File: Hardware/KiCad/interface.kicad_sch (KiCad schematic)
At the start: 36 parts, among them J2 STLink, J6 UART, J7 OLED, SW10 SW_Push_45deg, SW11 SW_Push_45deg, SW12 SW_Push_45deg, SW13 SW_Push_45deg, SW14 SW_Push_45deg, SW15 SW_Push_45deg, SW16 SW_Push_45deg, SW17 SW_Push_45deg, SW2 SW_Push_45deg, SW3 SW_Push_45deg, SW4 SW_Push_45deg, SW5 SW_Push_45deg, SW6 SW_Push_45deg, SW7 SW_Push_45deg, SW8 SW_Push_45deg, SW9 SW_Push_45deg

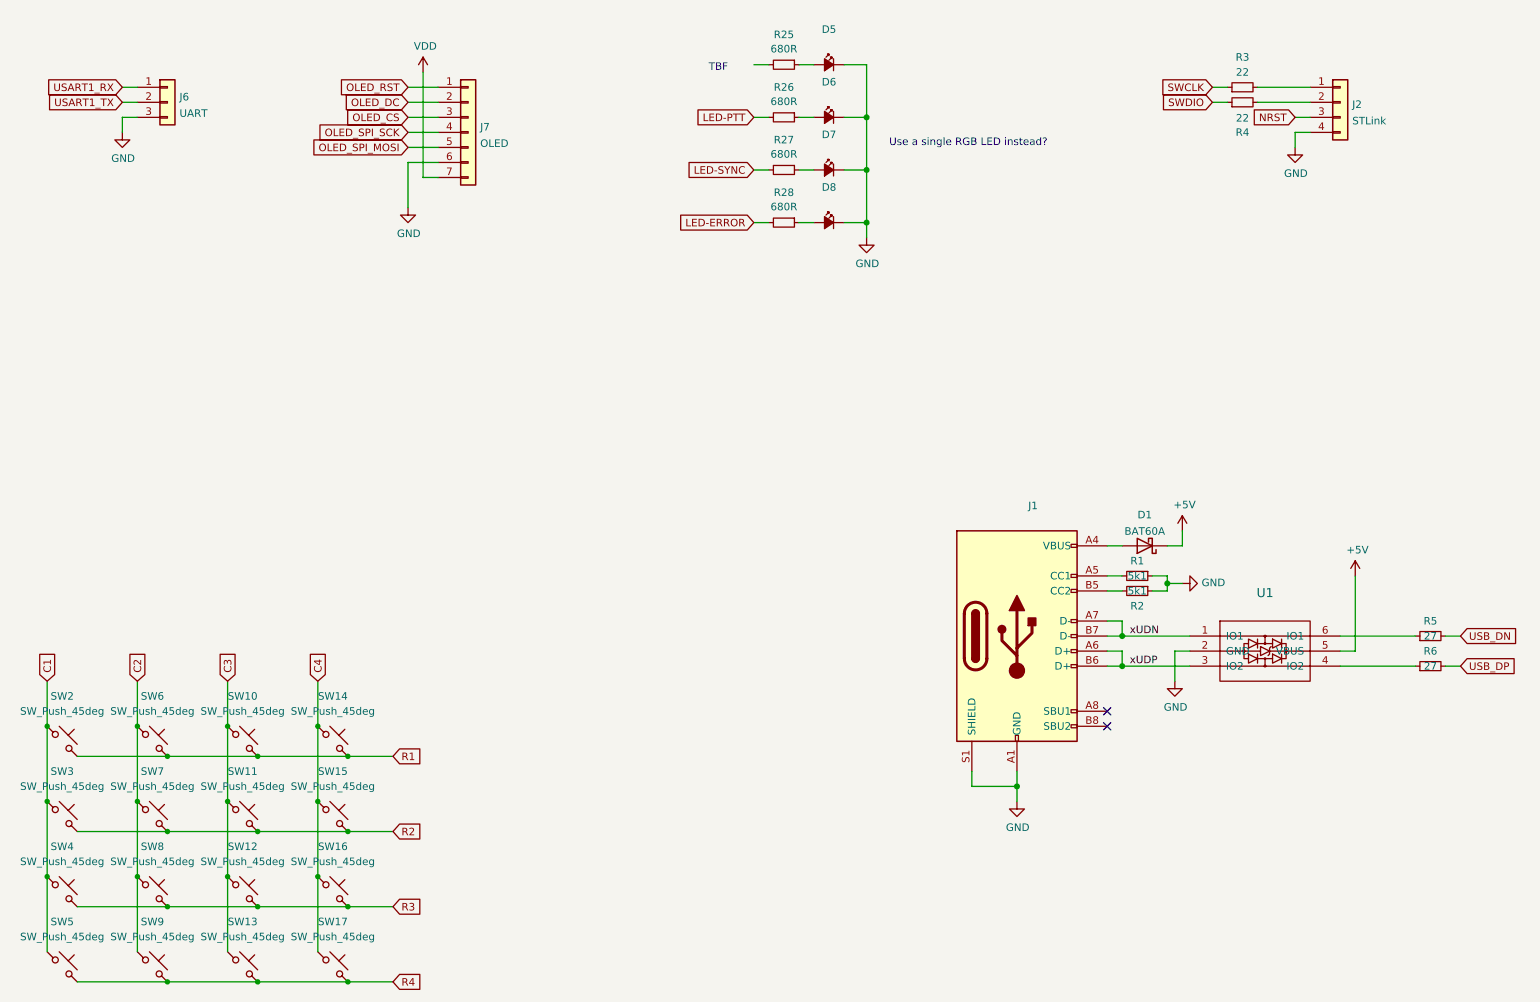
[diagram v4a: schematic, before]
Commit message: move cc1200 spi to spi-5 & update other labels throughout
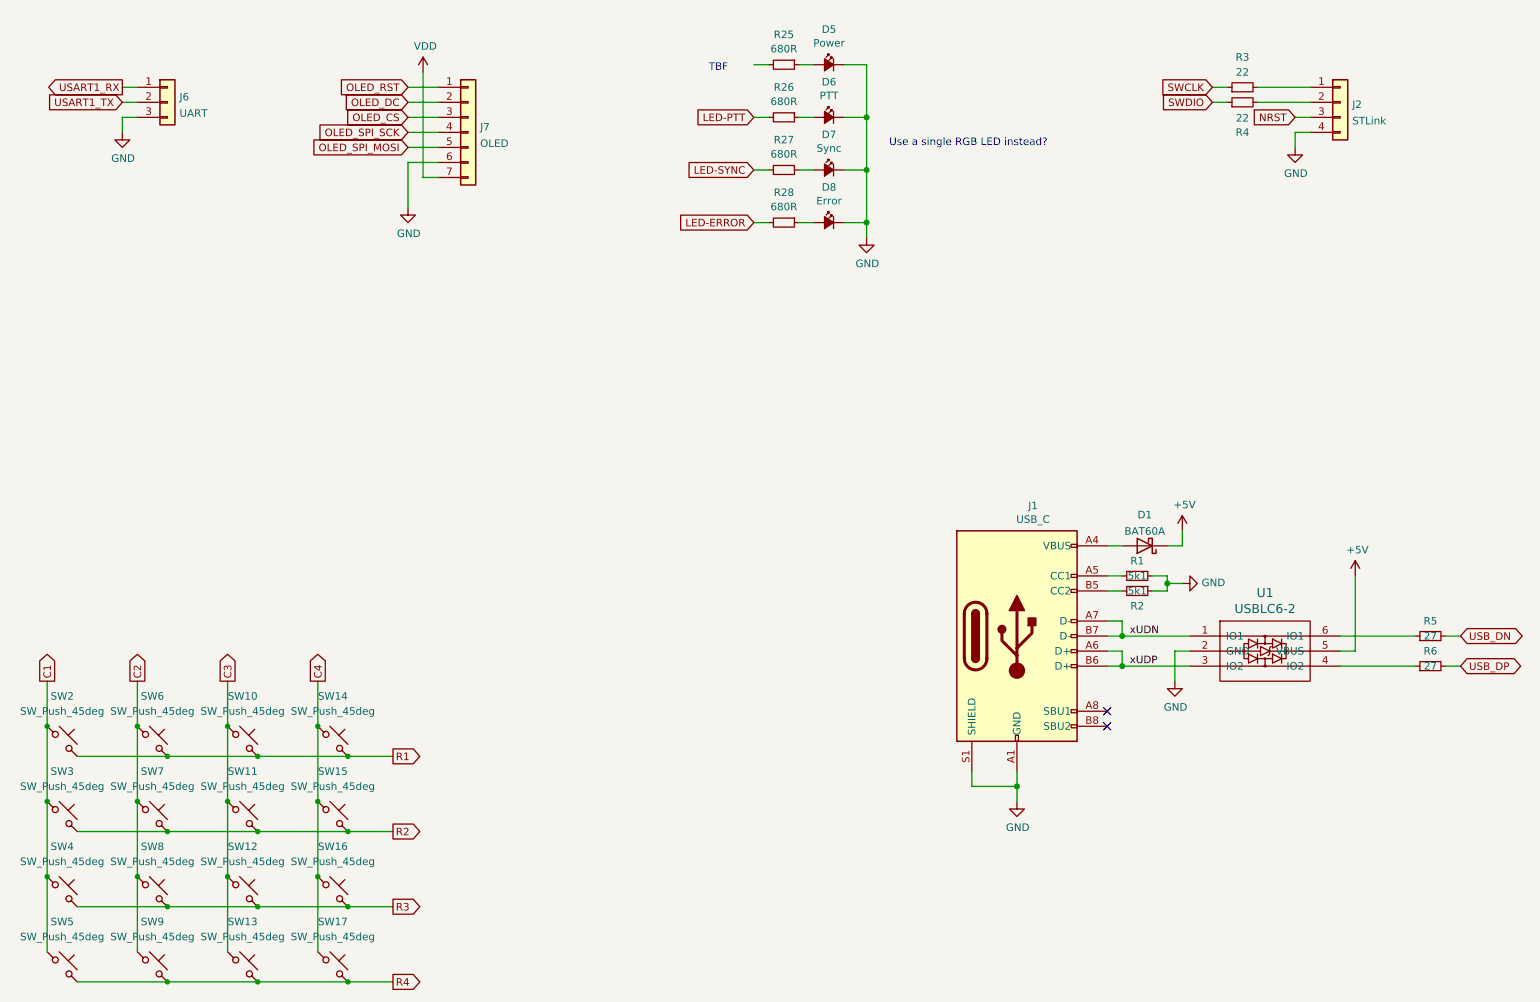
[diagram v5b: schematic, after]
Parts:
- D5: value (none) -> Power; footprint (none) -> Diode_SMD:D_0201_0603Metric
- D6: value (none) -> PTT; footprint (none) -> Diode_SMD:D_0603_1608Metric
- D7: value (none) -> Sync; footprint (none) -> Diode_SMD:D_0603_1608Metric
- D8: value (none) -> Error; footprint (none) -> Diode_SMD:D_0603_1608Metric
- J1: value (none) -> USB_C; footprint (none) -> Connector_USB:USB_C_Receptacle_HRO_TYPE-C-31-M-12
- U1: value (none) -> USBLC6-2; footprint (none) -> Package_TO_SOT_SMD:SOT-23-6
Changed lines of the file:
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@@
     )
   )
-  (global_label "USB_DN" (shape input) (at 266.7 128.27 0) (fields_autoplaced)
-    (effects (font (size 1.27 1.27)) (justify left))
-    (property "Intersheet References" "${INTERSHEET_REFS}" (id 0) (at -6.35 90.17 0)
-      (effects (font (size 1.27 1.27)) hide)
-    )
-  )
-  (global_label "C2" (shape input) (at 43.18 135.89 90) (fields_autoplaced)
+  (global_label "USB_DN" (shape bidirectional) (at 266.7 128.27 0) (fields_autoplaced)
+    (effects (font (size 1.27 1.27)) (justify left))
+    (property "Intersheet References" "${INTERSHEET_REFS}" (id 0) (at 276.4912 128.1906 0)
+      (effects (font (size 1.27 1.27)) (justify left) hide)
+    )
+  )
+  (global_label "C2" (shape output) (at 43.18 135.89 90) (fields_autoplaced)
     (effects (font (size 1.27 1.27)) (justify left))
     (property "Intersheet References" "${INTERSHEET_REFS}" (id 0) (at 43.1006 130.9974 90)
-      (effects (font (size 1.27 1.27)) (justify right) hide)
-    )
-  )
-  (global_label "R1" (shape input) (at 86.36 148.59 0) (fields_autoplaced)
+      (effects (font (size 1.27 1.27)) (justify left) hide)
+    )
+  )
+  (global_label "R1" (shape output) (at 86.36 148.59 0) (fields_autoplaced)
     (effects (font (size 1.27 1.27)) (justify left))
     (property "Intersheet References" "${INTERSHEET_REFS}" (id 0) (at 91.2526 148.5106 0)
@@
     )
   )
-  (global_label "R2" (shape input) (at 86.36 161.29 0) (fields_autoplaced)
+  (global_label "R2" (shape output) (at 86.36 161.29 0) (fields_autoplaced)
     (effects (font (size 1.27 1.27)) (justify left))
     (property "Intersheet References" "${INTERSHEET_REFS}" (id 0) (at 91.2526 161.2106 0)
@@
     )
   )
-  (global_label "C3" (shape input) (at 58.42 135.89 90) (fields_autoplaced)
+  (global_label "C3" (shape output) (at 58.42 135.89 90) (fields_autoplaced)
     (effects (font (size 1.27 1.27)) (justify left))
     (property "Intersheet References" "${INTERSHEET_REFS}" (id 0) (at 58.3406 130.9974 90)
-      (effects (font (size 1.27 1.27)) (justify right) hide)
+      (effects (font (size 1.27 1.27)) (justify left) hide)
     )
   )
@@
     )
   )
-  (global_label "R4" (shape input) (at 86.36 186.69 0) (fields_autoplaced)
+  (global_label "R4" (shape output) (at 86.36 186.69 0) (fields_autoplaced)
     (effects (font (size 1.27 1.27)) (justify left))
     (property "Intersheet References" "${INTERSHEET_REFS}" (id 0) (at 91.2526 186.6106 0)
@@
     )
   )
-  (global_label "C4" (shape input) (at 73.66 135.89 90) (fields_autoplaced)
+  (global_label "C4" (shape output) (at 73.66 135.89 90) (fields_autoplaced)
     (effects (font (size 1.27 1.27)) (justify left))
     (property "Intersheet References" "${INTERSHEET_REFS}" (id 0) (at 73.5806 130.9974 90)
+      (effects (font (size 1.27 1.27)) (justify left) hide)
+    )
+  )
+  (global_label "USART1_RX" (shape output) (at 40.64 35.56 180) (fields_autoplaced)
+    (effects (font (size 1.27 1.27)) (justify right))
+    (property "Intersheet References" "${INTERSHEET_REFS}" (id 0) (at 27.704 35.4806 0)
       (effects (font (size 1.27 1.27)) (justify right) hide)
     )
   )
-  (global_label "USART1_RX" (shape input) (at 40.64 35.56 180) (fields_autoplaced)
-    (effects (font (size 1.27 1.27)) (justify right))
-    (property "Intersheet References" "${INTERSHEET_REFS}" (id 0) (at 27.8437 35.6394 0)
-      (effects (font (size 1.27 1.27)) (justify right) hide)
-    )
-  )
-  (global_label "R3" (shape input) (at 86.36 173.99 0) (fields_autoplaced)
+  (global_label "R3" (shape output) (at 86.36 173.99 0) (fields_autoplaced)
     (effects (font (size 1.27 1.27)) (justify left))
     (property "Intersheet References" "${INTERSHEET_REFS}" (id 0) (at 91.2526 173.9106 0)
@@
     )
   )
-  (global_label "USB_DP" (shape input) (at 266.7 133.35 0) (fields_autoplaced)
-    (effects (font (size 1.27 1.27)) (justify left))
-    (property "Intersheet References" "${INTERSHEET_REFS}" (id 0) (at -6.35 90.17 0)
-      (effects (font (size 1.27 1.27)) hide)
+  (global_label "USB_DP" (shape bidirectional) (at 266.7 133.35 0) (fields_autoplaced)
+    (effects (font (size 1.27 1.27)) (justify left))
+    (property "Intersheet References" "${INTERSHEET_REFS}" (id 0) (at 276.4307 133.2706 0)
+      (effects (font (size 1.27 1.27)) (justify left) hide)
     )
   )
@@
     )
   )
-  (global_label "C1" (shape input) (at 27.94 135.89 90) (fields_autoplaced)
+  (global_label "C1" (shape output) (at 27.94 135.89 90) (fields_autoplaced)
     (effects (font (size 1.27 1.27)) (justify left))
     (property "Intersheet References" "${INTERSHEET_REFS}" (id 0) (at 27.8606 130.9974 90)
-      (effects (font (size 1.27 1.27)) (justify right) hide)
+      (effects (font (size 1.27 1.27)) (justify left) hide)
     )
   )
@@
       (effects (font (size 1.524 1.524)))
     )
-    (property "Value" "" (id 1) (at 233.68 123.6726 0)
-      (effects (font (size 1.524 1.524)))
-    )
-    (property "Footprint" "" (id 2) (at 233.68 130.81 0)
+    (property "Value" "USBLC6-2" (id 1) (at 233.68 123.6726 0)
+      (effects (font (size 1.524 1.524)))
+    )
+    (property "Footprint" "Package_TO_SOT_SMD:SOT-23-6" (id 2) (at 233.68 130.81 0)
       (effects (font (size 1.524 1.524)) hide)
     )
@@
     (in_bom yes) (on_board yes)
     (property "Reference" "D8" (id 0) (at 160.02 52.451 0))
-    (property "Value" "" (id 1) (at 160.02 54.7624 0))
-    (property "Footprint" "" (id 2) (at 160.02 58.42 90)
+    (property "Value" "Error" (id 1) (at 160.02 54.7624 0))
+    (property "Footprint" "Diode_SMD:D_0603_1608Metric" (id 2) (at 160.02 58.42 90)
       (effects (font (size 1.524 1.524)) hide)
     )
@@
     (in_bom yes) (on_board yes)
     (property "Reference" "D6" (id 0) (at 160.02 34.671 0))
-    (property "Value" "" (id 1) (at 160.02 36.9824 0))
-    (property "Footprint" "" (id 2) (at 160.02 40.64 90)
+    (property "Value" "PTT" (id 1) (at 160.02 36.9824 0))
+    (property "Footprint" "Diode_SMD:D_0603_1608Metric" (id 2) (at 160.02 40.64 90)
       (effects (font (size 1.524 1.524)) hide)
     )
@@
     (in_bom yes) (on_board yes)
     (property "Reference" "D7" (id 0) (at 160.02 43.561 0))
-    (property "Value" "" (id 1) (at 160.02 45.8724 0))
-    (property "Footprint" "" (id 2) (at 160.02 49.53 90)
+    (property "Value" "Sync" (id 1) (at 160.02 45.8724 0))
+    (property "Footprint" "Diode_SMD:D_0603_1608Metric" (id 2) (at 160.02 49.53 90)
       (effects (font (size 1.524 1.524)) hide)
     )
@@
     (in_bom yes) (on_board yes)
     (property "Reference" "D5" (id 0) (at 160.02 25.781 0))
-    (property "Value" "" (id 1) (at 160.02 28.0924 0))
-    (property "Footprint" "" (id 2) (at 160.02 31.75 90)
+    (property "Value" "Power" (id 1) (at 160.02 28.0924 0))
+    (property "Footprint" "Diode_SMD:D_0201_0603Metric" (id 2) (at 160.02 31.75 90)
       (effects (font (size 1.524 1.524)) hide)
     )
@@
     (in_bom yes) (on_board yes)
     (property "Reference" "J1" (id 0) (at 194.4878 106.2482 0))
-    (property "Value" "" (id 1) (at 194.4878 108.5596 0))
-    (property "Footprint" "" (id 2) (at 195.58 128.27 0)
-      (effects (font (size 1.27 1.27)) hide)
-    )
+    (property "Value" "USB_C" (id 1) (at 194.4878 108.5596 0))
+    (property "Footprint" "Connector_USB:USB_C_Receptacle_HRO_TYPE-C-31-M-12" (id 2) (at 195.58 128.27 0)
+      (effects (font (size 1.27 1.27)) hide)
+    )

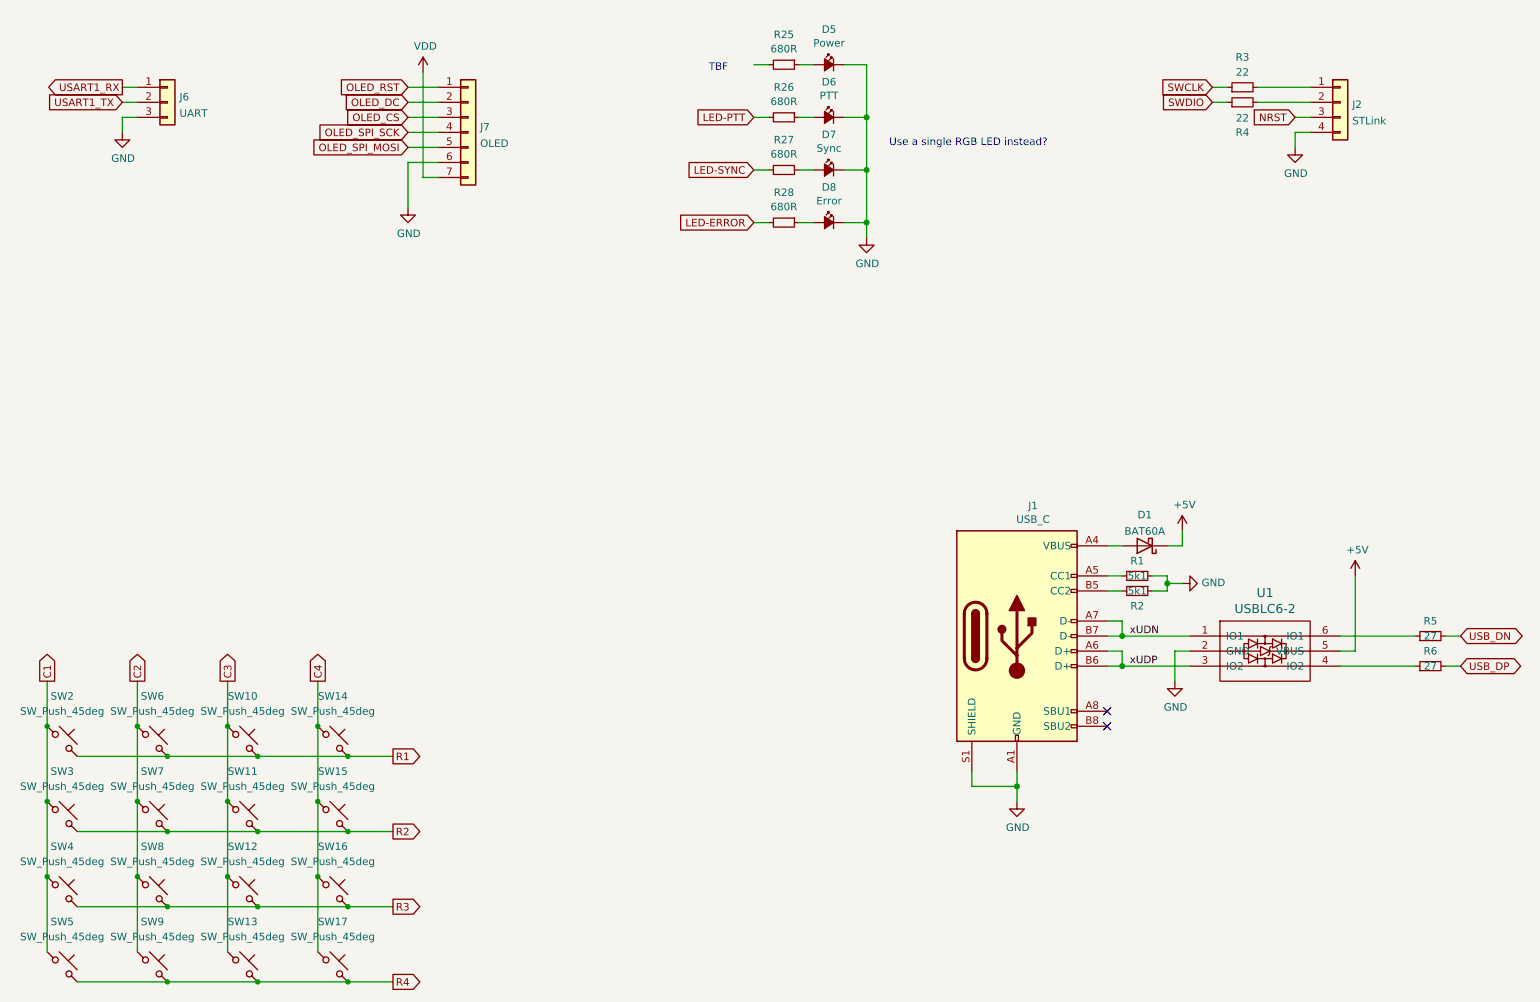
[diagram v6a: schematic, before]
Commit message: Use a single RGB LED
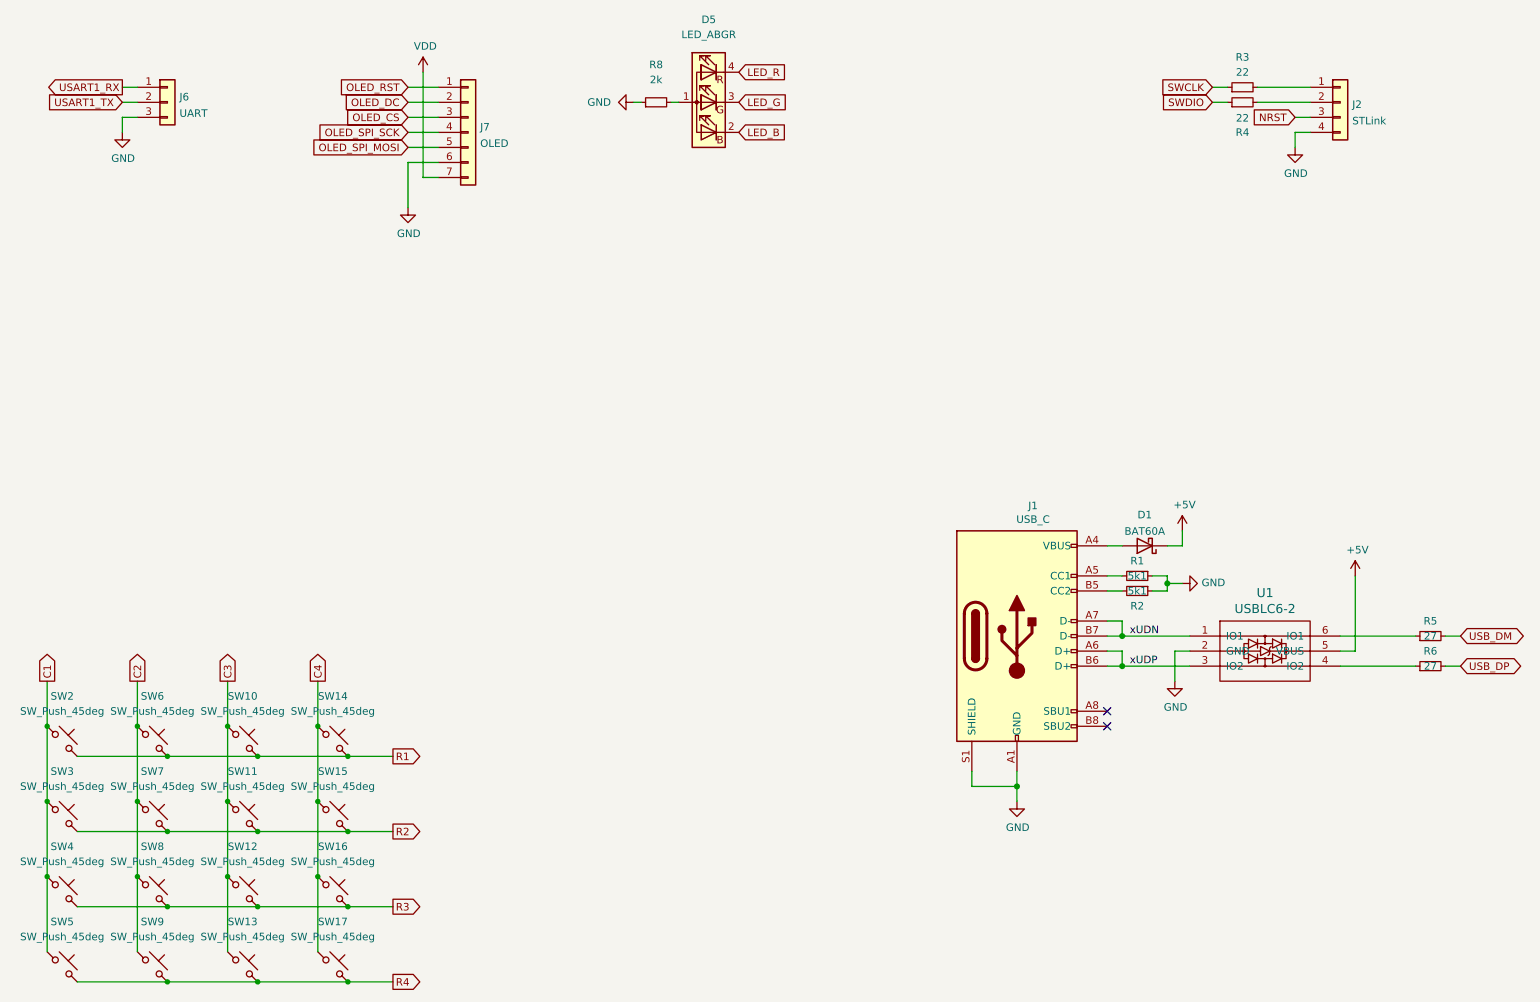
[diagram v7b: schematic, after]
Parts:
- removed D5: Power, Diode_SMD:D_0201_0603Metric, symbol pkl_device:pkl_Led_Small
- removed D6: PTT, Diode_SMD:D_0603_1608Metric, symbol pkl_device:pkl_Led_Small
- removed D7: Sync, Diode_SMD:D_0603_1608Metric, symbol pkl_device:pkl_Led_Small
- removed D8: Error, Diode_SMD:D_0603_1608Metric, symbol pkl_device:pkl_Led_Small
- removed R25, R26, R27, R28: 680R, Resistor_SMD:R_0402_1005Metric, symbol pkl_device:pkl_R_Small
- added D5: LED_ABGR, symbol Device:LED_ABGR
- added R8: 2k, symbol Device:R_Small
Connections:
- net GND: now also R8.1
- net USB_DN renamed USB_DM
- new net: D5.1 (A), R8.2
- new net LED_B: D5.2 (BK)
- new net LED_G: D5.3 (GK)
- new net LED_R: D5.4 (RK)
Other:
- note removed: "TBF"
- note removed: "Use a single RGB LED instead?"
